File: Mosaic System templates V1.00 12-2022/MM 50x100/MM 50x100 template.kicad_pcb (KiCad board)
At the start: 2 copper layers, 50 x 100 mm, 2 parts

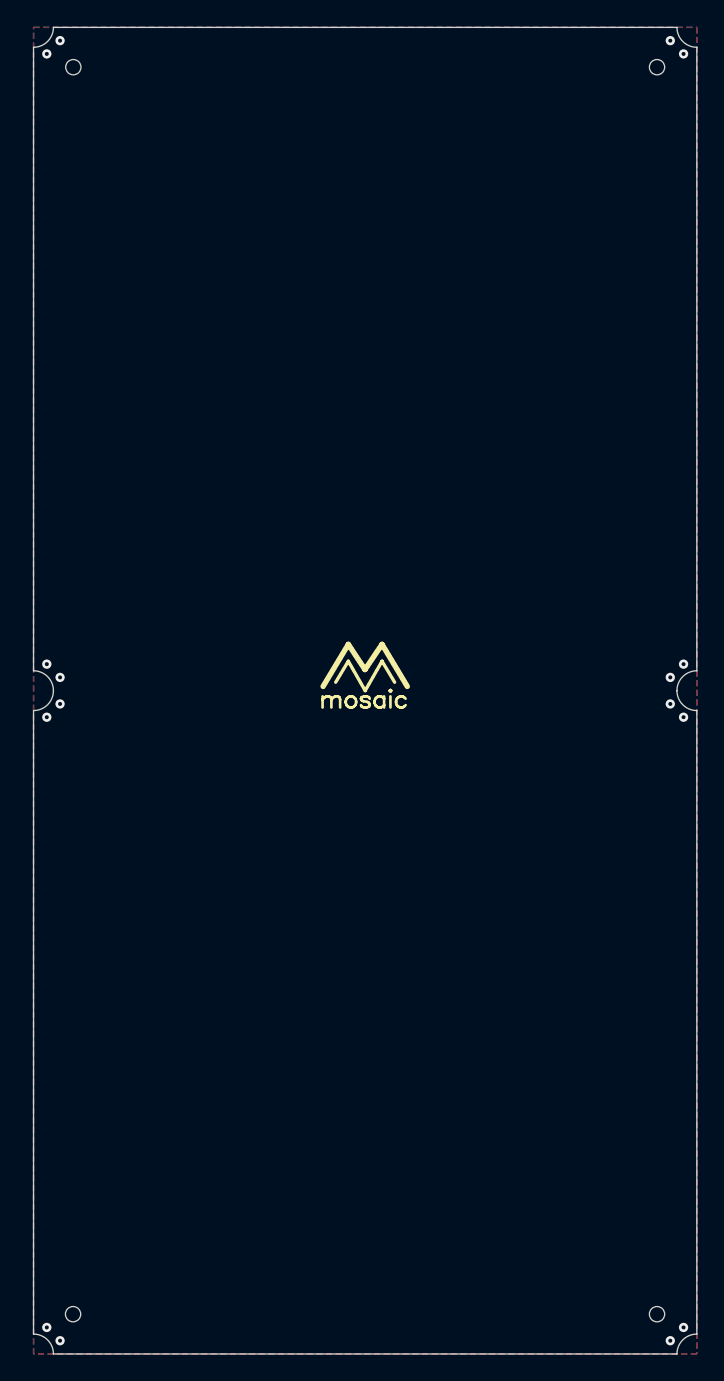
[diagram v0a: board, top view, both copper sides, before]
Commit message: V1.1
Clean up of some redundant footprints and added the correct polygons for the keepout area of the corners.
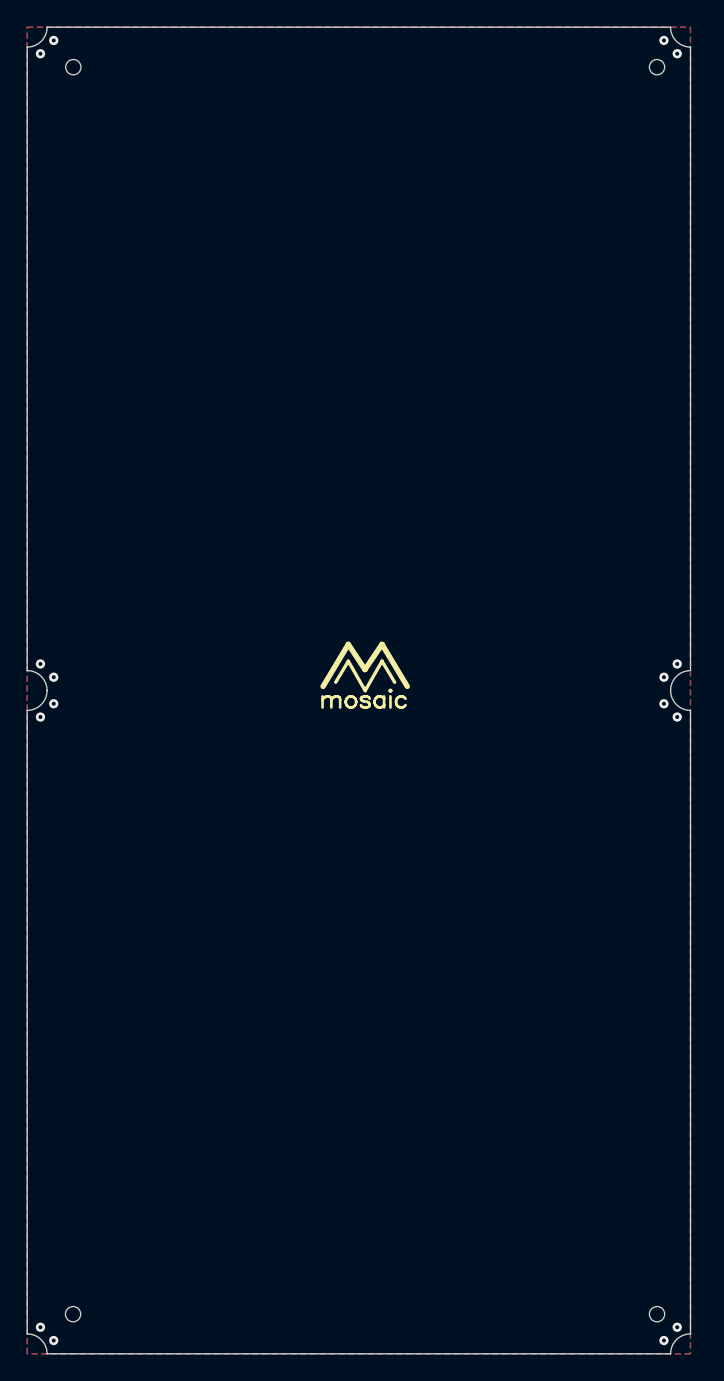
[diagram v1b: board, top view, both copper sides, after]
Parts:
- added REF4: copyright, 0-MM:copyright, F.Cu at (150.0, 145.0)

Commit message: update templates
Updated templates now have the current polygons for the soldermask keepout area and restrict any traces or components from entering those areas
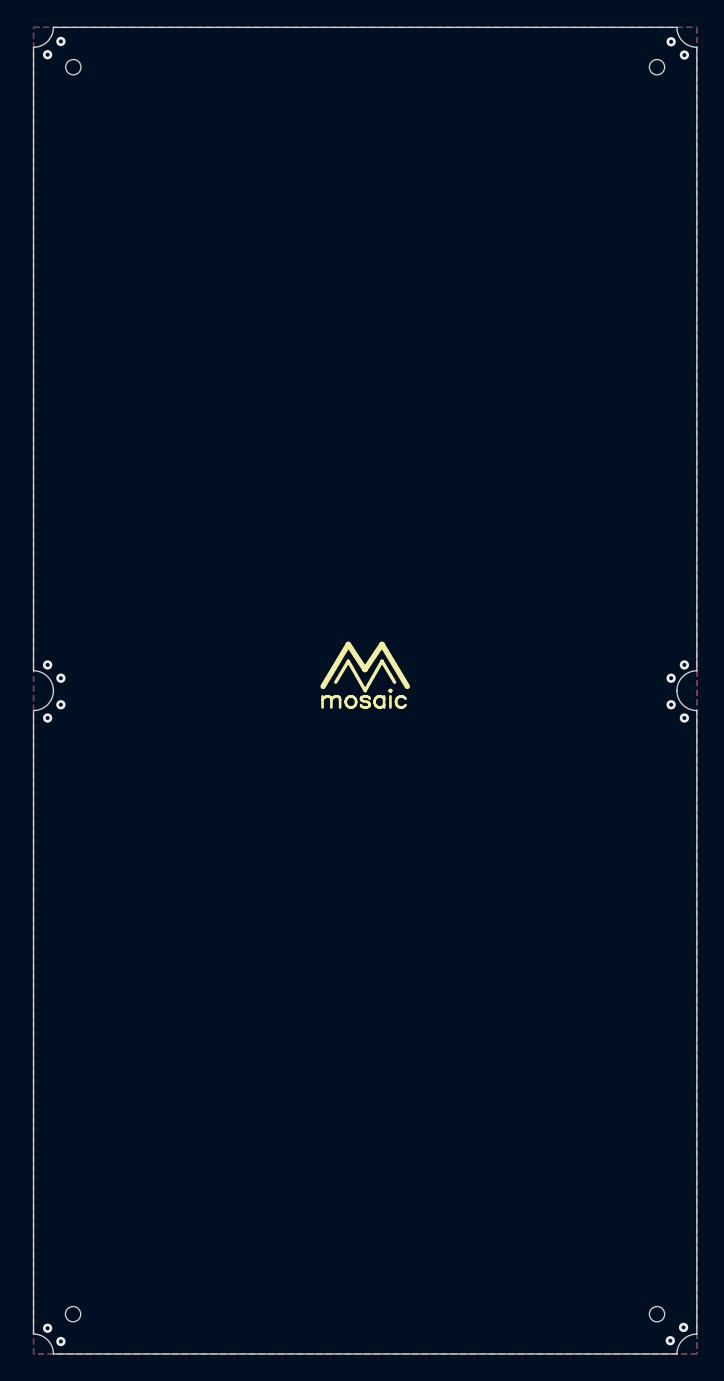
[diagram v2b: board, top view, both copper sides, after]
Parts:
- moved REF4 2.50 mm to (150.0, 147.5)
